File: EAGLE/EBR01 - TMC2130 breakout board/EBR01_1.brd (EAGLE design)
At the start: 26.7 x 25.4 mm, 24 parts, among them J1 CPL-CON-HEADER-0.1IN-8P-M, J2 CPL-CON-HEADER-0.1IN-8P-M, J3 CPL-CON-HEADER-0.1IN-2X3P-M, U2 CPL-REG-LIN-5V-0.1A

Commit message: Schematic tentative finalized.
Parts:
- removed C14, C15: 100nF, TinWhiskers:C0603
- removed R3: 0.22, TinWhiskers:R1206
- added C2: 0.33uF, TinWhiskers:C0603
- added C3: 100 nF, TinWhiskers:C0603
- added R1: 0.22, TinWhiskers:R1206
- C12, C13: value 470pF -> 100nF
- C4: value 0.1uF -> 100 nF
- C5: value 0.33uF -> 22 nF
- C7: value 22 nF -> 100 nF
- C8, C9: value 100 nF -> 470pF
- moved C4 84.1 mm to (54.6, 5.08)
- moved C7 48.7 mm to (45.7, 5.08)
- moved C8 37.0 mm to (8.89, 5.08)
- moved C5 27.9 mm to (-1.27, -7.62)
- moved C9 24.4 mm to (24.1, 16.5)
- moved C10 17.0 mm to (24.1, 12.7)
- moved C13 16.5 mm to (8.89, 2.54)
- moved C12 11.4 mm to (24.1, 1.27)
- moved C6 9.67 mm to (45.7, 8.89)
- moved C11 7.62 mm to (24.1, 8.89)
- moved R2 3.81 mm to (45.7, 12.7)
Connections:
- net 1A: now also C10.1; no longer C12.1
- net 1B: now also C11.1; no longer C13.1
- net 2A: now also C9.1; no longer C11.1
- net 2B: now also C8.1; no longer C10.1
- net GND: now also C2.1, C3.1, C6.2, C7.2, R1.1; no longer C14.2, C15.2, C4.1, C5.1, R3.1
- net N$1: now also C5.2; no longer C7.2
- net N$3: now also C12.1, R1.2; no longer C14.1, R2.2
- net N$4: now also C13.1, R2.2; no longer C15.1, R3.2
- net N$5: now also C5.1; no longer C7.1
- net N$8: now also C4.1; no longer C6.1
- net VCC: now also C3.2; no longer C4.2
- net VMOT: now also C2.2, C4.2, C6.1, C7.1; no longer C5.2, C6.2, C8.1, C9.1
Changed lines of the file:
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@@
 <attribute name="VALUE" x="11.07" y="9.36" size="0.95" layer="27" ratio="10"/>
 </element>
-<element name="C6" library="TinWhiskers" package="C0603" value="100 nF" x="54.61" y="5.08"/>
+<element name="C4" library="TinWhiskers" package="C0603" value="100 nF" x="54.61" y="5.08"/>
 <element name="C1" library="TinWhiskers" package="C0603" value="470 nF" x="54.61" y="1.27"/>
-<element name="R2" library="TinWhiskers" package="R1206" value="0.22" x="45.72" y="16.51"/>
-<element name="R3" library="TinWhiskers" package="R1206" value="0.22" x="45.72" y="12.7"/>
-<element name="C8" library="TinWhiskers" package="C0603" value="100 nF" x="45.72" y="8.89"/>
-<element name="C9" library="TinWhiskers" package="C0603" value="100 nF" x="45.72" y="5.08"/>
+<element name="R1" library="TinWhiskers" package="R1206" value="0.22" x="45.72" y="16.51"/>
+<element name="R2" library="TinWhiskers" package="R1206" value="0.22" x="45.72" y="12.7"/>
+<element name="C6" library="TinWhiskers" package="C0603" value="100 nF" x="45.72" y="8.89"/>
+<element name="C7" library="TinWhiskers" package="C0603" value="100 nF" x="45.72" y="5.08"/>
 <element name="D1" library="TinWhiskers" package="MICRO-SMP" value="MSS1P6" x="41.91" y="2.54"/>
 <element name="D2" library="TinWhiskers" package="MICRO-SMP" value="MSS1P6" x="38.1" y="2.54"/>
 <element name="D3" library="TinWhiskers" package="MICRO-SMP" value="MSS1P6" x="34.29" y="2.54"/>
 <element name="D4" library="TinWhiskers" package="MICRO-SMP" value="MSS1P6" x="30.48" y="2.54"/>
-<element name="C10" library="TinWhiskers" package="C0603" value="470pF" x="8.89" y="5.08"/>
-<element name="C11" library="TinWhiskers" package="C0603" value="470pF" x="24.13" y="16.51"/>
-<element name="C12" library="TinWhiskers" package="C0603" value="470pF" x="24.13" y="12.7"/>
-<element name="C13" library="TinWhiskers" package="C0603" value="470pF" x="24.13" y="8.89"/>
-<element name="C15" library="TinWhiskers" package="C0603" value="100nF" x="8.89" y="2.54"/>
-<element name="C14" library="TinWhiskers" package="C0603" value="100nF" x="24.13" y="1.27"/>
-<element name="C7" library="TinWhiskers" package="C0603" value="22 nF" x="-1.27" y="-7.62"/>
+<element name="C8" library="TinWhiskers" package="C0603" value="470pF" x="8.89" y="5.08"/>
+<element name="C9" library="TinWhiskers" package="C0603" value="470pF" x="24.13" y="16.51"/>
+<element name="C10" library="TinWhiskers" package="C0603" value="470pF" x="24.13" y="12.7"/>
+<element name="C11" library="TinWhiskers" package="C0603" value="470pF" x="24.13" y="8.89"/>
+<element name="C13" library="TinWhiskers" package="C0603" value="100nF" x="8.89" y="2.54"/>
+<element name="C12" library="TinWhiskers" package="C0603" value="100nF" x="24.13" y="1.27"/>
+<element name="C5" library="TinWhiskers" package="C0603" value="22 nF" x="-1.27" y="-7.62"/>
 <element name="J2" library="TinWhiskers" package="CON-HDR-8POS-MALE" value="CPL-CON-HEADER-0.1IN-8P-M" x="6.35" y="-13.97" smashed="yes">
 <attribute name="NAME" x="9.15" y="-12.07" size="1.27" layer="25" ratio="12"/>
@@
 <attribute name="NAME" x="-21.02" y="-22.48" size="1.27" layer="25" font="vector" ratio="12"/>
 </element>
-<element name="C5" library="TinWhiskers" package="C0603" value="0.33uF" x="-20.32" y="-27.94"/>
-<element name="C4" library="TinWhiskers" package="C0603" value="0.1uF" x="-20.32" y="-33.02"/>
+<element name="C2" library="TinWhiskers" package="C0603" value="0.33uF" x="-20.32" y="-27.94"/>
+<element name="C3" library="TinWhiskers" package="C0603" value="100 nF" x="-20.32" y="-33.02"/>
 </elements>
 <signals>
@@
 </signal>
 <signal name="VMOT">
-<contactref element="C6" pad="2"/>
-<contactref element="C8" pad="1"/>
-<contactref element="C9" pad="1"/>
+<contactref element="C4" pad="2"/>
+<contactref element="C6" pad="1"/>
+<contactref element="C7" pad="1"/>
 <contactref element="J2" pad="1"/>
 <contactref element="U1" pad="31"/>
@@
 <contactref element="C1" pad="2"/>
 <contactref element="U2" pad="1"/>
-<contactref element="C5" pad="2"/>
+<contactref element="C2" pad="2"/>
 <wire x1="55.335" y1="1.27" x2="55.335" y2="5.08" width="0" layer="19" extent="1-1"/>
 <wire x1="44.995" y1="5.08" x2="55.335" y2="5.08" width="0" layer="19" extent="1-1"/>
@@
 <contactref element="U1" pad="15"/>
 <contactref element="D1" pad="NEG"/>
-<contactref element="C10" pad="1"/>
+<contactref element="C8" pad="1"/>
 <contactref element="J2" pad="3"/>
 <wire x1="8.165" y1="5.08" x2="40.91" y2="2.54" width="0" layer="19" extent="1-1"/>
@@
 <contactref element="U1" pad="13"/>
 <contactref element="D2" pad="NEG"/>
-<contactref element="C11" pad="1"/>
+<contactref element="C9" pad="1"/>
 <contactref element="J2" pad="4"/>
 <wire x1="23.405" y1="16.51" x2="37.1" y2="2.54" width="0" layer="19" extent="1-1"/>
@@
 <contactref element="U1" pad="32"/>
 <contactref element="D3" pad="NEG"/>
-<contactref element="C12" pad="1"/>
+<contactref element="C10" pad="1"/>
 <contactref element="J2" pad="5"/>
 <wire x1="23.405" y1="12.7" x2="33.29" y2="2.54" width="0" layer="19" extent="1-1"/>
@@
 <contactref element="U1" pad="34"/>
 <contactref element="D4" pad="NEG"/>
-<contactref element="C13" pad="1"/>
+<contactref element="C11" pad="1"/>
 <contactref element="J2" pad="6"/>
 <wire x1="23.405" y1="8.89" x2="29.48" y2="2.54" width="0" layer="19" extent="1-1"/>
@@
 <contactref element="C1" pad="1"/>
 <contactref element="U1" pad="36"/>
+<contactref element="R1" pad="1"/>
 <contactref element="R2" pad="1"/>
-<contactref element="R3" pad="1"/>
+<contactref element="C6" pad="2"/>
+<contactref element="C7" pad="2"/>
 <contactref element="C8" pad="2"/>
 <contactref element="C9" pad="2"/>
@@
 <contactref element="C12" pad="2"/>
 <contactref element="C13" pad="2"/>
-<contactref element="C14" pad="2"/>
-<contactref element="C15" pad="2"/>
 <contactref element="J2" pad="2"/>
 <contactref element="J2" pad="8"/>
-<contactref element="C4" pad="1"/>
 <contactref element="U2" pad="2"/>
-<contactref element="C5" pad="1"/>
+<contactref element="C2" pad="1"/>
+<contactref element="C3" pad="1"/>
 <wire x1="44.52" y1="12.7" x2="44.52" y2="16.51" width="0" layer="19" extent="1-1"/>
 <wire x1="46.445" y1="8.89" x2="44.52" y2="12.7" width="0" layer="19" extent="1-1"/>
@@
 <contactref element="U1" pad="8"/>
 <contactref element="U2" pad="3"/>
-<contactref element="C4" pad="2"/>
+<contactref element="C3" pad="2"/>
 <wire x1="-18.82" y1="-19.78" x2="-19.595" y2="-33.02" width="0" layer="19" extent="1-1"/>
 <wire x1="5.32" y1="8.91" x2="-18.82" y2="-19.78" width="0" layer="19" extent="1-1"/>
@@
 <signal name="N$1">
 <contactref element="U1" pad="28"/>
-<contactref element="C7" pad="2"/>
+<contactref element="C5" pad="2"/>
 <wire x1="-0.545" y1="-7.62" x2="9.92" y2="12.41" width="0" layer="19" extent="1-1"/>
 </signal>
 <signal name="N$5">
 <contactref element="U1" pad="27"/>
-<contactref element="C7" pad="1"/>
+<contactref element="C5" pad="1"/>
 <wire x1="-1.995" y1="-7.62" x2="9.92" y2="11.91" width="0" layer="19" extent="1-1"/>
 </signal>
 <signal name="N$8">
 <contactref element="U1" pad="29"/>
-<contactref element="C6" pad="1"/>
+<contactref element="C4" pad="1"/>
 <wire x1="9.37" y1="12.96" x2="53.885" y2="5.08" width="0" layer="19" extent="1-1"/>
 </signal>
@@
 <contactref element="D1" pad="POS"/>
 <contactref element="D2" pad="POS"/>
-<contactref element="R2" pad="2"/>
+<contactref element="R1" pad="2"/>
 <contactref element="U1" pad="33"/>
-<contactref element="C14" pad="1"/>
+<contactref element="C12" pad="1"/>
 <wire x1="42.95" y1="2.54" x2="46.92" y2="16.51" width="0" layer="19" extent="1-1"/>
 <wire x1="39.14" y1="2.54" x2="42.95" y2="2.54" width="0" layer="19" extent="1-1"/>
@@
 <contactref element="D3" pad="POS"/>
 <contactref element="D4" pad="POS"/>
-<contactref element="R3" pad="2"/>
+<contactref element="R2" pad="2"/>
 <contactref element="U1" pad="14"/>
-<contactref element="C15" pad="1"/>
+<contactref element="C13" pad="1"/>
 <wire x1="35.33" y1="2.54" x2="46.92" y2="12.7" width="0" layer="19" extent="1-1"/>
 <wire x1="31.52" y1="2.54" x2="35.33" y2="2.54" width="0" layer="19" extent="1-1"/>

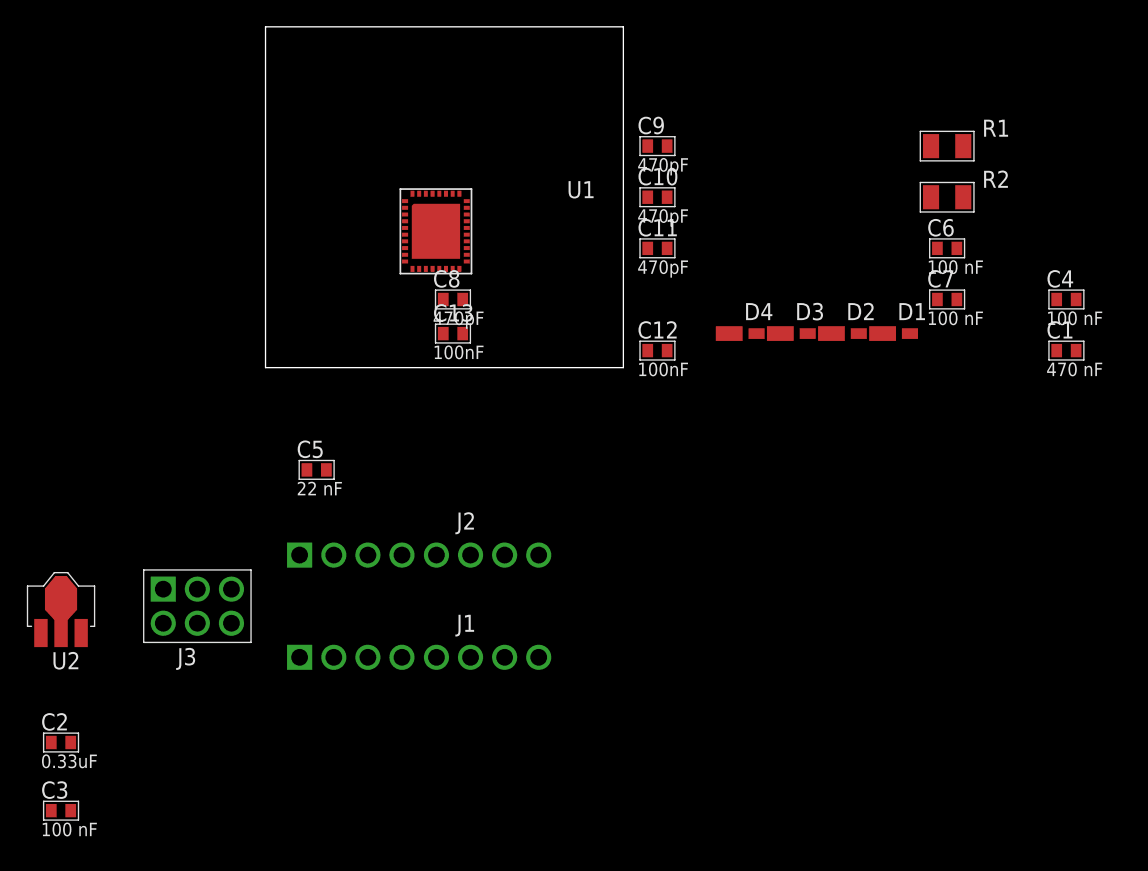
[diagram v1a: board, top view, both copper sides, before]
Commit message: Breakout board layout
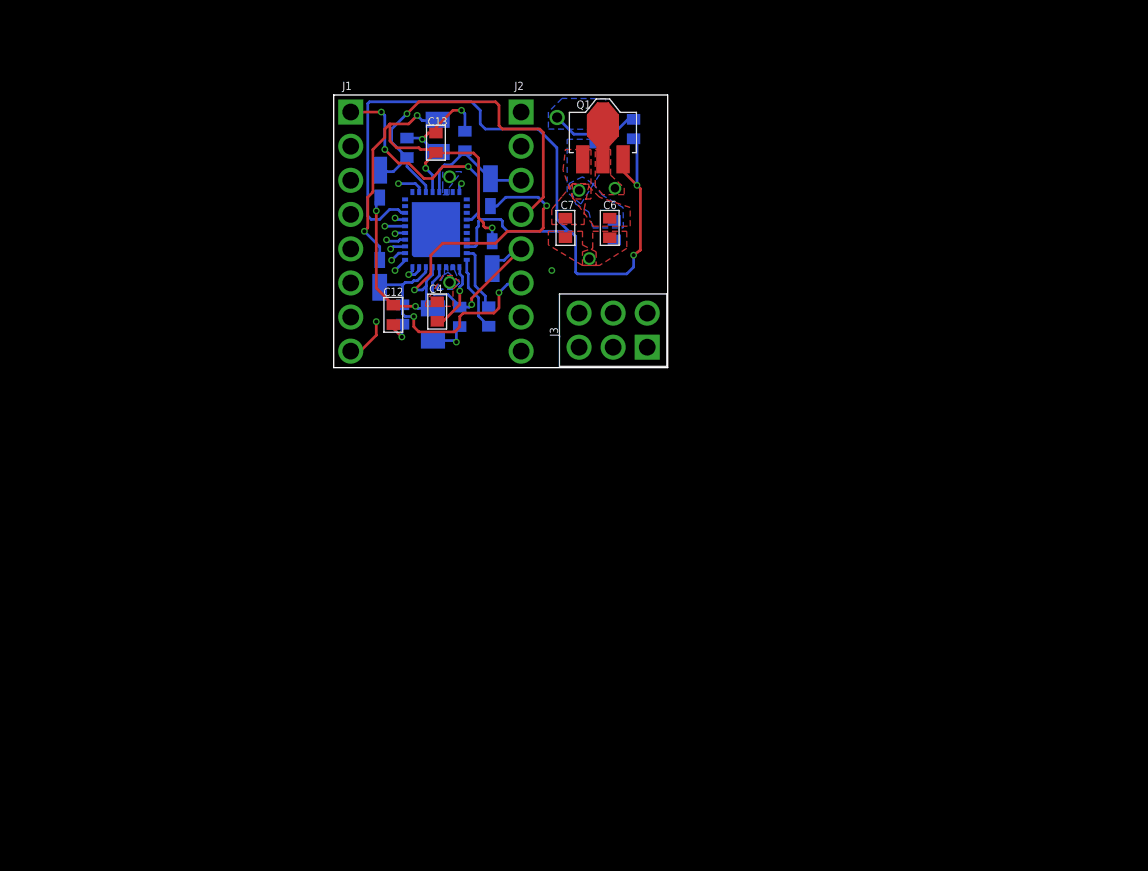
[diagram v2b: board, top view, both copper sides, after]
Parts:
- removed U2: CPL-REG-LIN-5V-0.1A, TinWhiskers:SOT-89
- added Q1: CPL-REG-LIN-5V-0.1A, TinWhiskers:SOT-89
- U1: value (none) -> TMC2130-LA
- moved C3 66.3 mm to (22.4, 17.8), flipped to the bottom, turned to 270 degrees
- moved C2 60.4 mm to (19.6, 17.5), flipped to the bottom, turned to 270 degrees
- moved C4 46.9 mm to (7.71, 4.18), turned to 90 degrees
- moved R1 40.6 mm to (7.40, 3.22), flipped to the bottom, turned to 90 degrees
- moved R2 38.2 mm to (7.75, 17.3), flipped to the bottom, turned to 90 degrees
- moved J3 37.2 mm to (20.8, 2.79), turned to 180 degrees
- moved D2 36.4 mm to (3.43, 13.7), flipped to the bottom, turned to 270 degrees
- moved C1 34.9 mm to (20.9, 10.2), flipped to the bottom, turned to 90 degrees
- moved J1 32.2 mm to (1.27, 10.2), turned to 270 degrees
- moved D1 32.0 mm to (11.7, 13.1), flipped to the bottom, turned to 270 degrees
- moved C7 28.9 mm to (17.3, 10.4), turned to 270 degrees
- moved D4 27.4 mm to (3.43, 6.99), flipped to the bottom, turned to 90 degrees
- moved J2 25.3 mm to (14.0, 10.2), turned to 270 degrees
- moved C6 25.2 mm to (20.6, 10.4), turned to 270 degrees
- moved D3 23.2 mm to (11.8, 8.38), flipped to the bottom, turned to 90 degrees
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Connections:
- net GND: now also Q1.2, U1.PAD; no longer U1.VSS, U2.2
- net VCC: now also Q1.3; no longer U2.3
- net VMOT: now also Q1.1; no longer U2.1
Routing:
- net VCC: track 0.00 -> 64.8 mm, vias 0 -> 2
- net N$3: track 0.00 -> 35.2 mm, vias 0 -> 4
- net N$4: track 0.00 -> 34.7 mm, vias 0 -> 4
- net 2A: track 0.00 -> 29.2 mm, vias 0 -> 1
- net GND: track 0.00 -> 24.9 mm, vias 0 -> 10
- net SPI_SDO: track 0.00 -> 24.6 mm, vias 0 -> 1
- net SPI_SCK: track 0.00 -> 21.0 mm, vias 0 -> 2
- net SPI_!CS!: track 0.00 -> 19.9 mm, vias 0 -> 1
- net 1B: track 0.00 -> 18.9 mm, vias 0 -> 2
- net !ENABLE!: track 0.00 -> 17.5 mm, vias 0 -> 3
- net DIR: track 0.00 -> 16.6 mm, vias 0 -> 2
- net 1A: track 0.00 -> 14.4 mm, vias 0 -> 1
- net STEP: track 0.00 -> 10.1 mm, vias 0 -> 1
- net 2B: track 0.00 -> 9.28 mm
- net N$1: track 0.00 -> 5.63 mm
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- added copper zone on layer 1, net GND
- added copper zone on layer 16, net GND
- added copper zone on layer 2, net GND
- added copper zone on layer 1, net VMOT
- added copper zone on layer 15, net VMOT
- added copper zone on layer 16, net VMOT
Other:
- board size 26.7 x 25.4 mm -> 24.9 x 20.3 mm

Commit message: Routing done.
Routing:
- net SPI_SDI: track 1.47 -> 30.0 mm, vias 1 -> 3
- net CLK: track 1.11 -> 26.1 mm, vias 1 -> 2
- net VCC: track 64.8 -> 63.6 mm, vias 2 -> 4
- net GND: track 24.9 -> 25.6 mm, vias 10 -> 20

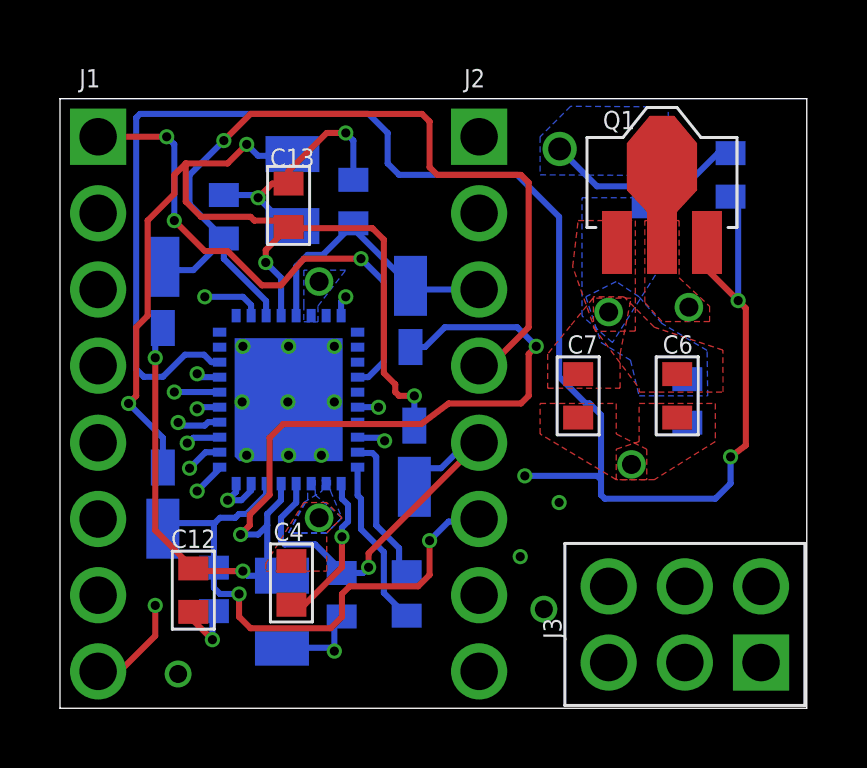
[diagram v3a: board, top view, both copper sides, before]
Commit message: Trace widths for motor lines increased to handle 2A current. Eliminated/approved all DRC errors except those for Q1, which remain for review by Neil. Refined DRC check to reflect manufacturing specs for HQPCB. The new DRC file will be saved in FPD-Electronics repo ASAP. Board is ready for Gerber export. ECAM01 schematic added connections for pending USB OTG component.
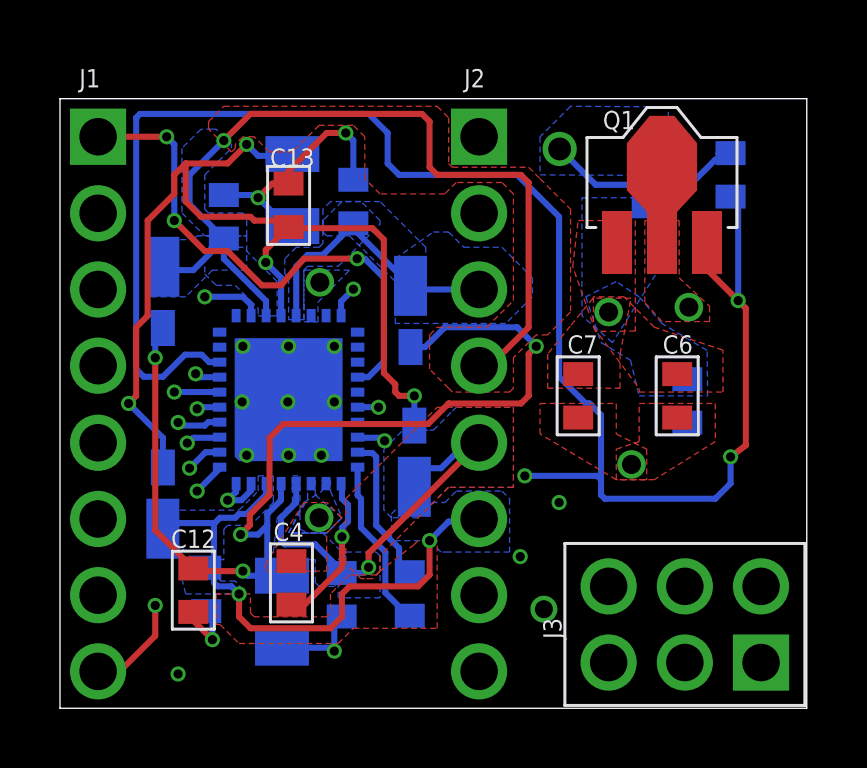
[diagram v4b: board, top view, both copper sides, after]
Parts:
- moved C11 0.25 mm to (4.88, 3.96)
- moved C5 0.10 mm to (11.7, 3.81)
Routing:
- net GND: track 25.6 -> 26.5 mm
- added copper zone on layer 1, net 1A
- added copper zone on layer 16, net 1A
- added copper zone on layer 1, net 1B
- added copper zone on layer 16, net 1B
- added copper zone on layer 1, net 2A
- added copper zone on layer 16, net 2A
- added copper zone on layer 16, net 2B
